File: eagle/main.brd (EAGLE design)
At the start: 100 x 95 mm, 33 parts, among them IC1 STM32F103, IC2 LM1117, Q1 8MHz

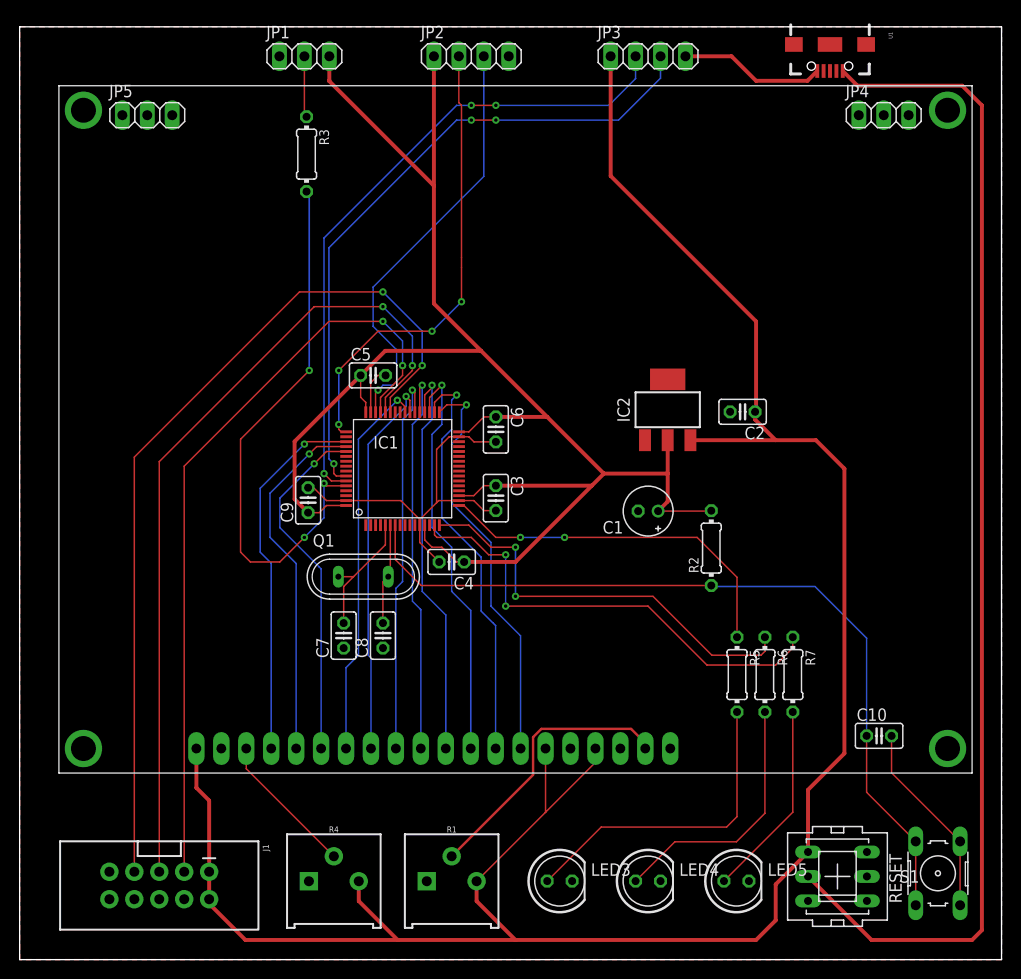
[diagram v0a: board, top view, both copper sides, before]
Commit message: Add silkscreen labels
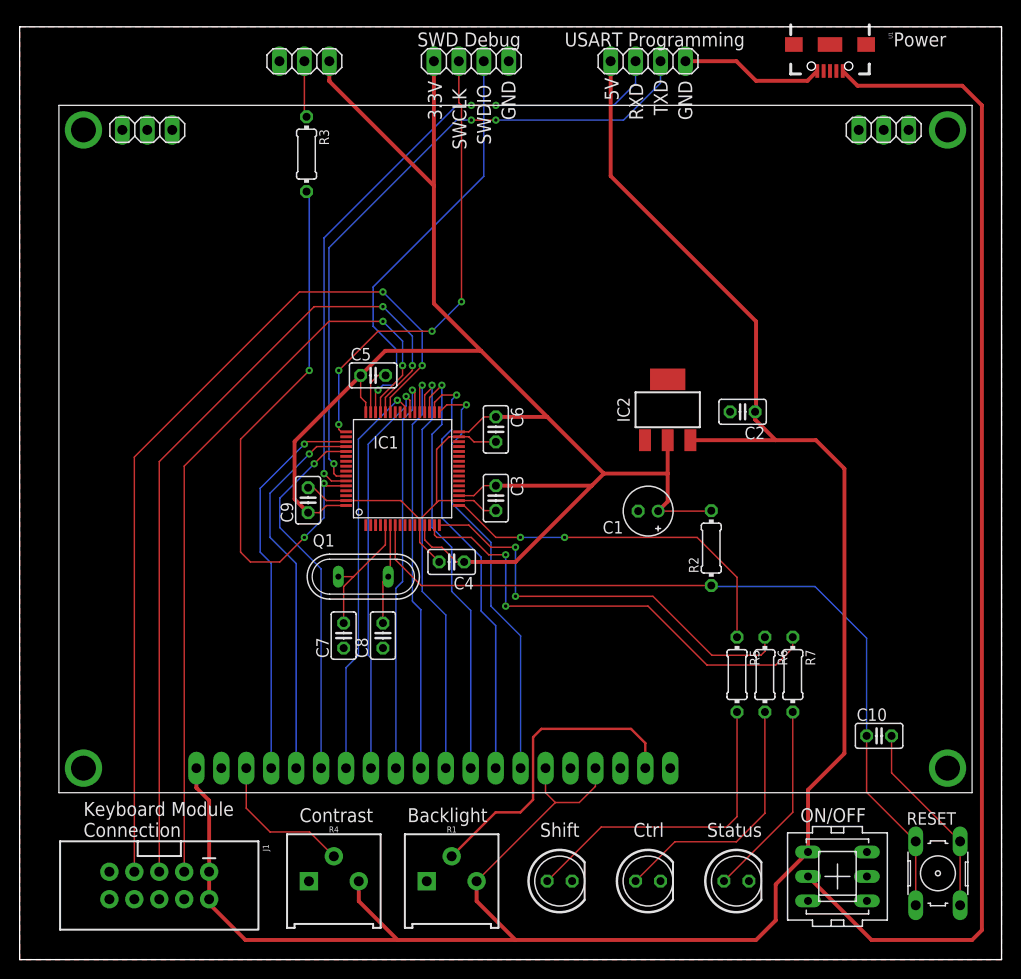
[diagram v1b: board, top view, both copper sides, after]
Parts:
- LED4: value ORANGE -> ONG
- LED5: value GREEN -> GRN
- moved GLCD2 2.00 mm to (4.00, 17.0)
- moved JP4 1.50 mm to (88.0, 84.5)
- moved JP5 1.50 mm to (13.0, 84.5)
- moved JP1 0.50 mm to (29.0, 91.5)
- moved JP2 0.50 mm to (46.0, 91.5)
- moved JP3 0.50 mm to (64.0, 91.5)
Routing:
- net VCC: track 228.6 -> 223.0 mm
- net N$1: track 28.5 -> 32.0 mm
- net DB7: track 41.6 -> 43.6 mm
- net DB6: track 42.5 -> 44.5 mm
- net RW: track 36.8 -> 38.8 mm
- net RS: track 37.7 -> 39.7 mm
- net EN: track 36.0 -> 38.0 mm
- net DB5: track 42.3 -> 44.3 mm
- net DB4: track 41.5 -> 43.5 mm
- net DB3: track 40.6 -> 42.6 mm
- net DB2: track 39.5 -> 41.5 mm
- net DB1: track 39.3 -> 41.3 mm
- net DB0: track 39.3 -> 41.3 mm
- net 3.3V: track 173.6 -> 172.6 mm
- net SWDIO: track 43.4 -> 42.9 mm
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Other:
- board text added: "0"
- board text added: "1"
- board text added: "3.3V"
- board text added: "5V"
- board text added: "BOOT0"
- board text added: "Backlight"
- board text added: "Contrast"
- board text added: "Ctrl"
- board text added: "GND"
- board text added: "Keyboard Module Connection"
- board text added: "ON/OFF"
- board text added: "Power"
- board text added: "RXD"
- board text added: "SWCLK"
- board text added: "SWD Debug"
- board text added: "SWDIO"
- board text added: "Shift"
- board text added: "Status"
- board text added: "TXD"
- board text added: "USART Programming"
